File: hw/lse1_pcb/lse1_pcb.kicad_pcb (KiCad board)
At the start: 4 copper layers, 79.4 x 95.6 mm, 73 parts, among them J1 PWR_IN, J3 DataOut, M1 Motor_3pin, Q1 IRFR1205, Q2 IRFR1205, Q3 IRFR1205, Q4 IRFR1205, Q5 IRFR1205, Q6 IRFR1205, U1 IR2301, U2 IR2301, U3 IR2301, U4 AZ1084CD-5.0TRG1, U5 LM339, U6 EK-TM4C123GXL

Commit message: start code project + correct pcb
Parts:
- removed MEAS1, MEAS2, MEAS3, NEUT: TestPoint, Connector_PinHeader_2.54mm:PinHeader_1x01_P2.54mm_Vertical
- added J10: TP_NEUT, Connector_PinHeader_2.54mm:PinHeader_1x02_P2.54mm_Vertical, F.Cu at (167.2, 81.5)
- added J11: TP_FASE2, Connector_PinHeader_2.54mm:PinHeader_1x02_P2.54mm_Vertical, F.Cu at (209.3, 56.4)
- added J12: TP_FASE1, Connector_PinHeader_2.54mm:PinHeader_1x02_P2.54mm_Vertical, F.Cu at (184.7, 55.7)
- added J13: TP_FASE3, Connector_PinHeader_2.54mm:PinHeader_1x02_P2.54mm_Vertical, F.Cu at (234.5, 56.6)
- added J2: TP_DIV1, Connector_PinHeader_2.54mm:PinHeader_1x02_P2.54mm_Vertical, F.Cu at (184.9, 69.7)
- added J4: TP_DIV2, Connector_PinHeader_2.54mm:PinHeader_1x02_P2.54mm_Vertical, F.Cu at (209.6, 69.7)
- added J5: TP_DIV3, Connector_PinHeader_2.54mm:PinHeader_1x02_P2.54mm_Vertical, F.Cu at (234.5, 69.7)
- added J6: TP_MEAS, Connector_PinHeader_2.54mm:PinHeader_2x03_P2.54mm_Vertical, F.Cu at (168.4, 103.6)
- added J7: TPG2, Connector_PinHeader_2.54mm:PinHeader_1x04_P2.54mm_Vertical, F.Cu at (189.8, 66.0)
- added J8: TPG1, Connector_PinHeader_2.54mm:PinHeader_1x04_P2.54mm_Vertical, F.Cu at (165.4, 66.0)
- added J9: TPG3, Connector_PinHeader_2.54mm:PinHeader_1x04_P2.54mm_Vertical, F.Cu at (214.7, 66.2)
- R18, R19, R20, R21, R22, R23: moved to B.Cu
- moved R19 5.67 mm to (178.7, 76.0)
- moved Rpull0 4.74 mm to (184.1, 99.8), turned to 0 degrees
- moved R20 4.46 mm to (203.0, 76.1), turned to 0 degrees
- moved R22 3.95 mm to (226.5, 71.9)
- moved R10 3.70 mm to (224.0, 77.1)
- moved R11 3.70 mm to (219.5, 66.1)
- moved R9 3.70 mm to (221.5, 77.1)
- moved CBOOT3 3.70 mm to (217.7, 64.5)
- moved Cd3 3.70 mm to (230.0, 67.7)
- moved Cdec6 3.70 mm to (230.0, 70.0)
- moved D3 3.70 mm to (217.7, 68.5)
- moved Q5 3.70 mm to (220.3, 58.3)
- moved Q6 3.70 mm to (228.5, 58.3)
- moved R12 3.70 mm to (226.2, 67.2)
- moved U3 3.70 mm to (222.0, 71.1)
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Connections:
- net Net-(Q1-G) renamed G1A
- net Net-(Q2-G) renamed G1B
- net Net-(Q3-G) renamed G2A
- net Net-(Q4-G) renamed G2B
- net Net-(Q5-G) renamed G3A
- net Net-(Q6-G) renamed G3B
- Rpull0 pad 2: +5V -> +3.3V
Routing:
- net +5V: track 50.9 -> 19.3 mm
- net G1B: track 2.46 -> 16.9 mm
- net G2B: track 2.41 -> 15.0 mm
- net G3B: track 2.39 -> 14.9 mm
- net Net-(J2-Pin_1): track 27.9 -> 39.1 mm
- net Net-(J4-Pin_1): track 25.4 -> 34.1 mm, vias 1 -> 0
- net Net-(J5-Pin_1): track 45.9 -> 53.9 mm, vias 1 -> 0
- net FASE3: track 31.9 -> 39.7 mm
- net GND: track 12.0 -> 6.30 mm, vias 615 -> 626
- net FASE1: track 32.0 -> 37.6 mm
- net FASE2: track 20.7 -> 25.9 mm
- net G2A: track 2.64 -> 6.10 mm
- net G1A: track 2.78 -> 6.24 mm
- net G3A: track 2.72 -> 6.14 mm
- net Net-(D5-K): track 0.00 -> 3.23 mm
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
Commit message: update silkscreen
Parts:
- added G***: LOGO, maqueen_pics:plane_face_inv, F.Cu at (200.0, 57.0)
- added G***: LOGO, maqueen_pics:face, F.Cu at (199.0, 97.0)
- added G***: LOGO, maqueen_pics:planes_logo, F.Cu at (200.0, 60.0)
- renumbered J2 to COMP1, J4 to COMP2, J5 to COMP3, J3 to DATAOUT1, J8 to JTPG1, J7 to JTPG2, J6 to MEAS, J10 to NEUT1, J9 to TPG3
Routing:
- net FASE2: track 25.9 -> 24.2 mm
- net FASE1: track 37.6 -> 36.0 mm
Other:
- board text added: "1"
- board text added: "1A"
- board text added: "1B"
- board text added: "2"
- board text added: "2A"
- board text added: "2B"
- board text added: "3"
- board text added: "3A"
- board text added: "3B"
- board text added: "ADRIÀ BRÚ MIQUEL LIMÓN LSE1"
- board text added: "CLK"
- board text added: "CS"
- board text added: "RX"
- board text added: "TX"

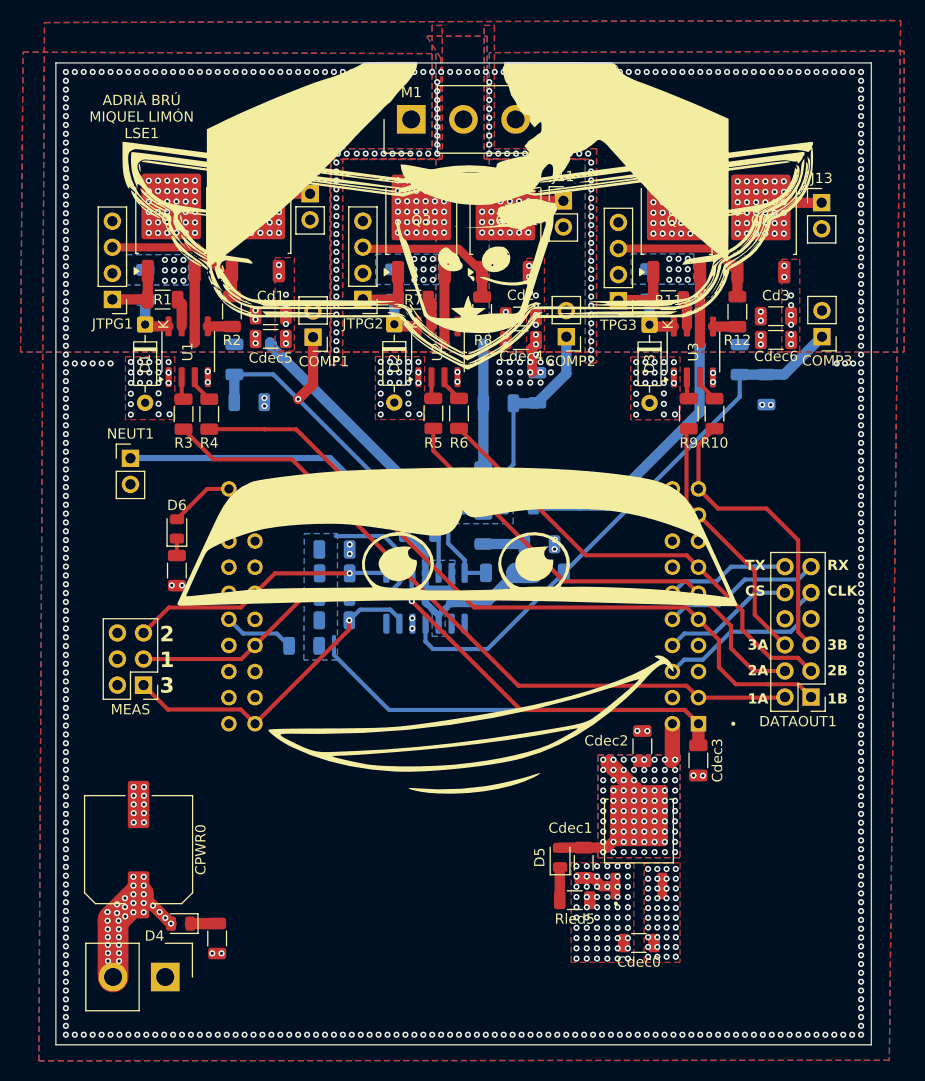
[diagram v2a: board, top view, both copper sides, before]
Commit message: finish silkscreen
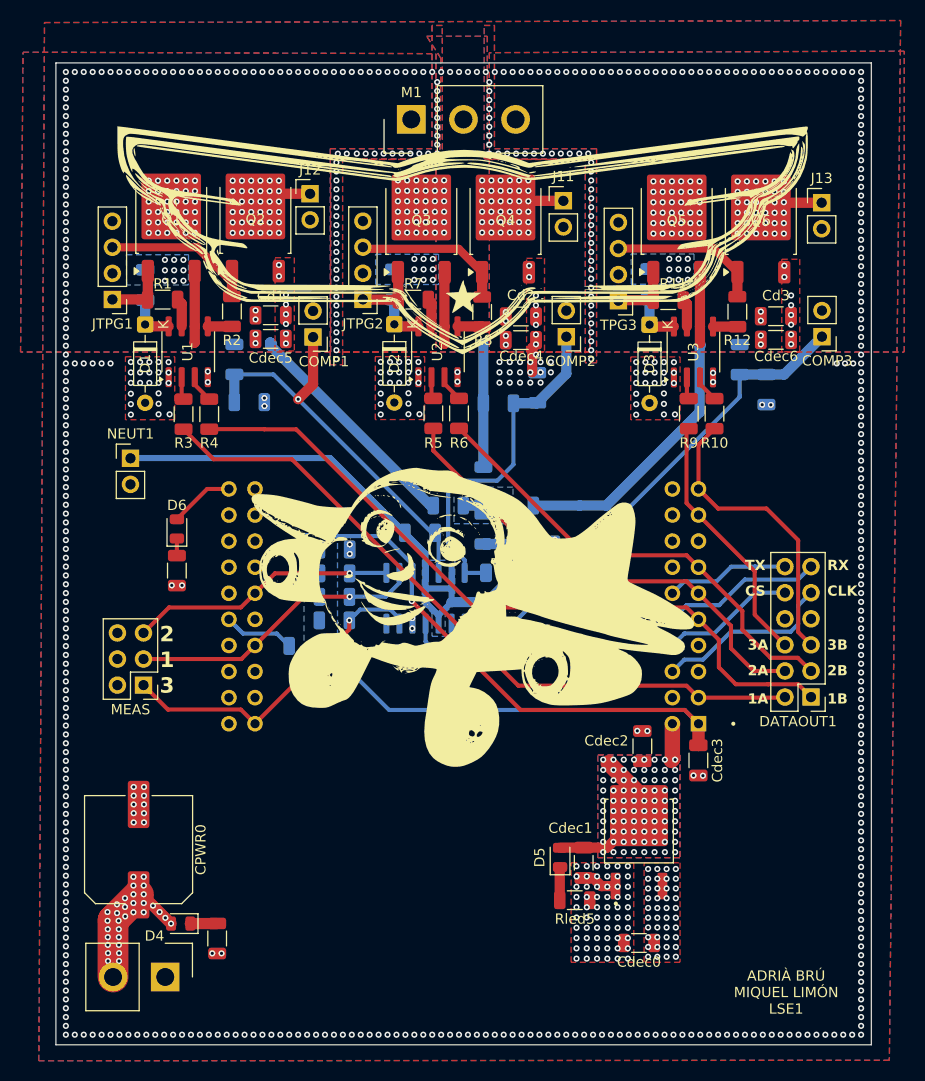
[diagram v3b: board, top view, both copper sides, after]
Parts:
- removed the G*** at (200.0, 57.0)
- removed the G*** at (199.0, 97.0)
- added G***: LOGO, maqueen_pics:peepoPlane, F.Cu at (200.5, 97.0)
- added G***: LOGO, maqueen_pics:peepoPlane, B.Cu at (191.0, 120.5)
- moved G*** 1.58 mm to (199.5, 58.5)
